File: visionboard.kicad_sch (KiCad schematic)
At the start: 1 part, among them U1 Hirose DF40C-100DS-0.4V

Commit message: microSD card
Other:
- added sheet MicroSD Card (MicroSD.kicad_sch)
- added sheet RJ45 (RJ45.kicad_sch)
- moved on the sheet: U1A, U1B, U1C

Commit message: usb work cont
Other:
- sheet MicroSD Card renamed USB2
- sheet USB2: file MicroSD.kicad_sch -> USB2.kicad_sch
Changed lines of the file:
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@@
 			(color 0 0 0 0.0000)
 		)
-		(property "Sheetname" "MicroSD Card"
+		(property "Sheetname" "USB2"
 			(at 0 304.0884 0)
 			(effects
@@
 			)
 		)
-		(property "Sheetfile" "MicroSD.kicad_sch"
+		(property "Sheetfile" "USB2.kicad_sch"
 			(at 0 337.1346 0)
 			(effects

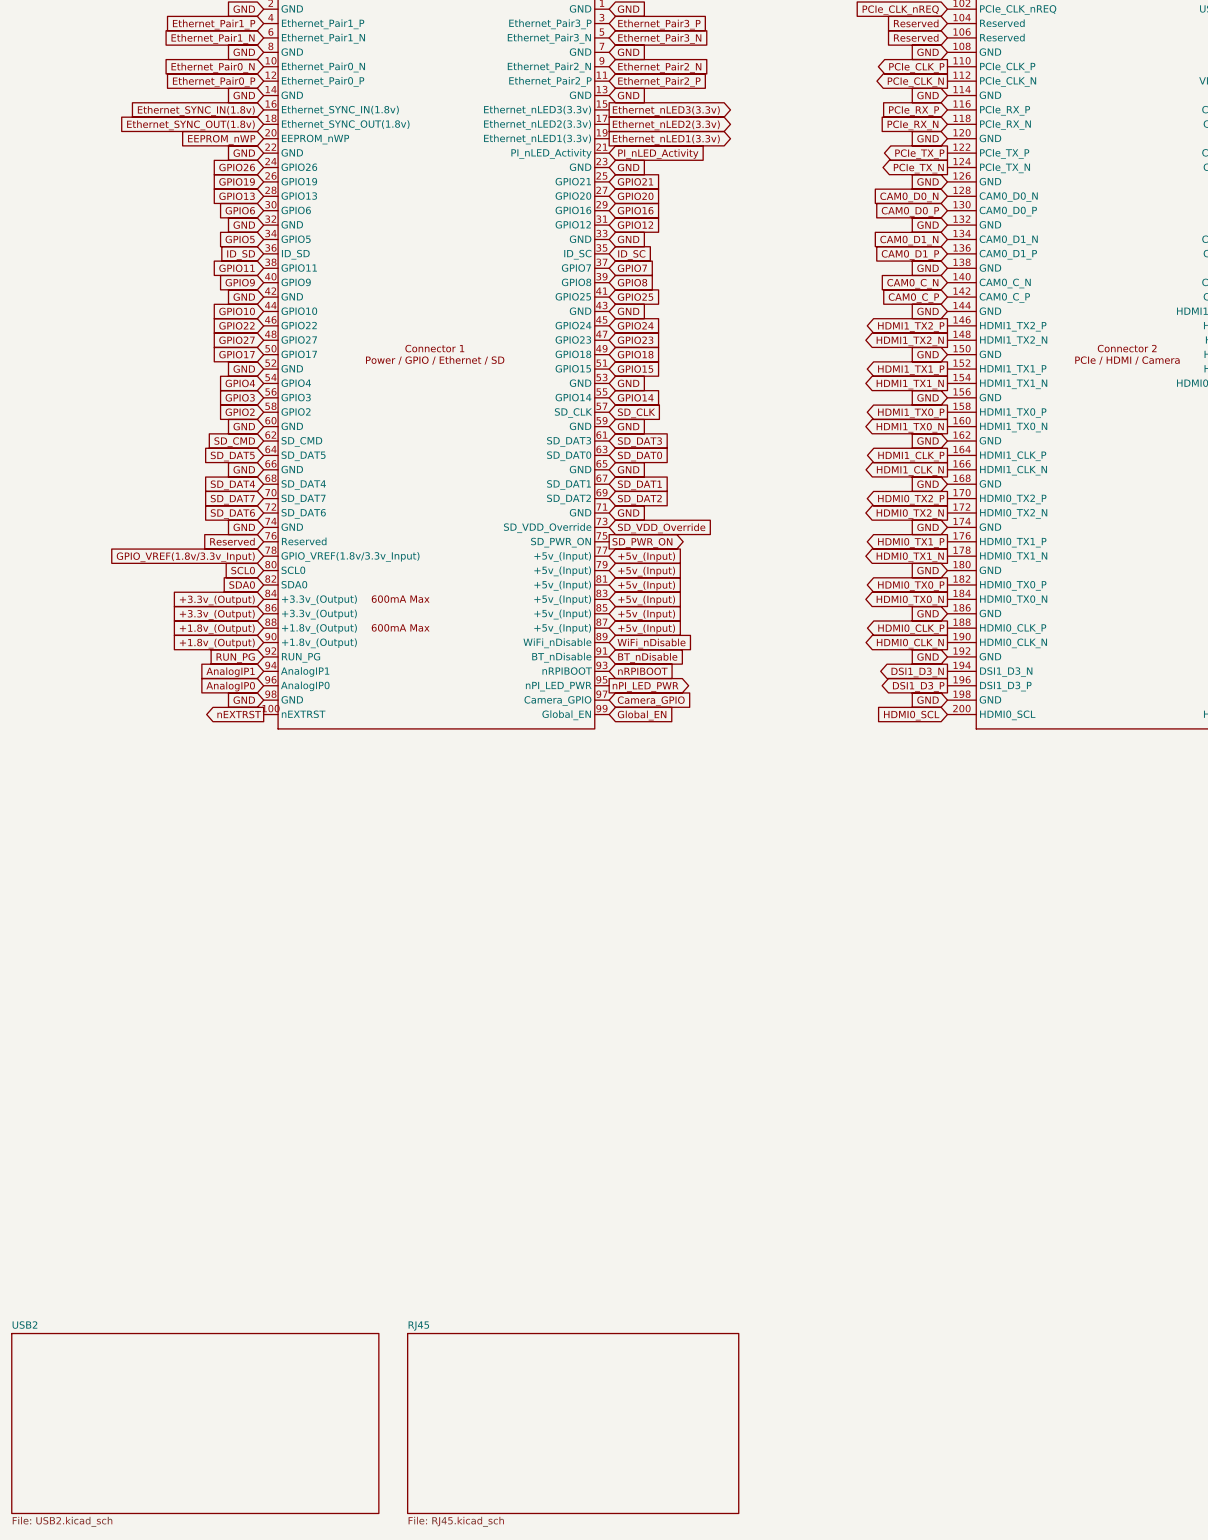
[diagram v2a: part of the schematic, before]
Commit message: usb2 fixes and usb3 started
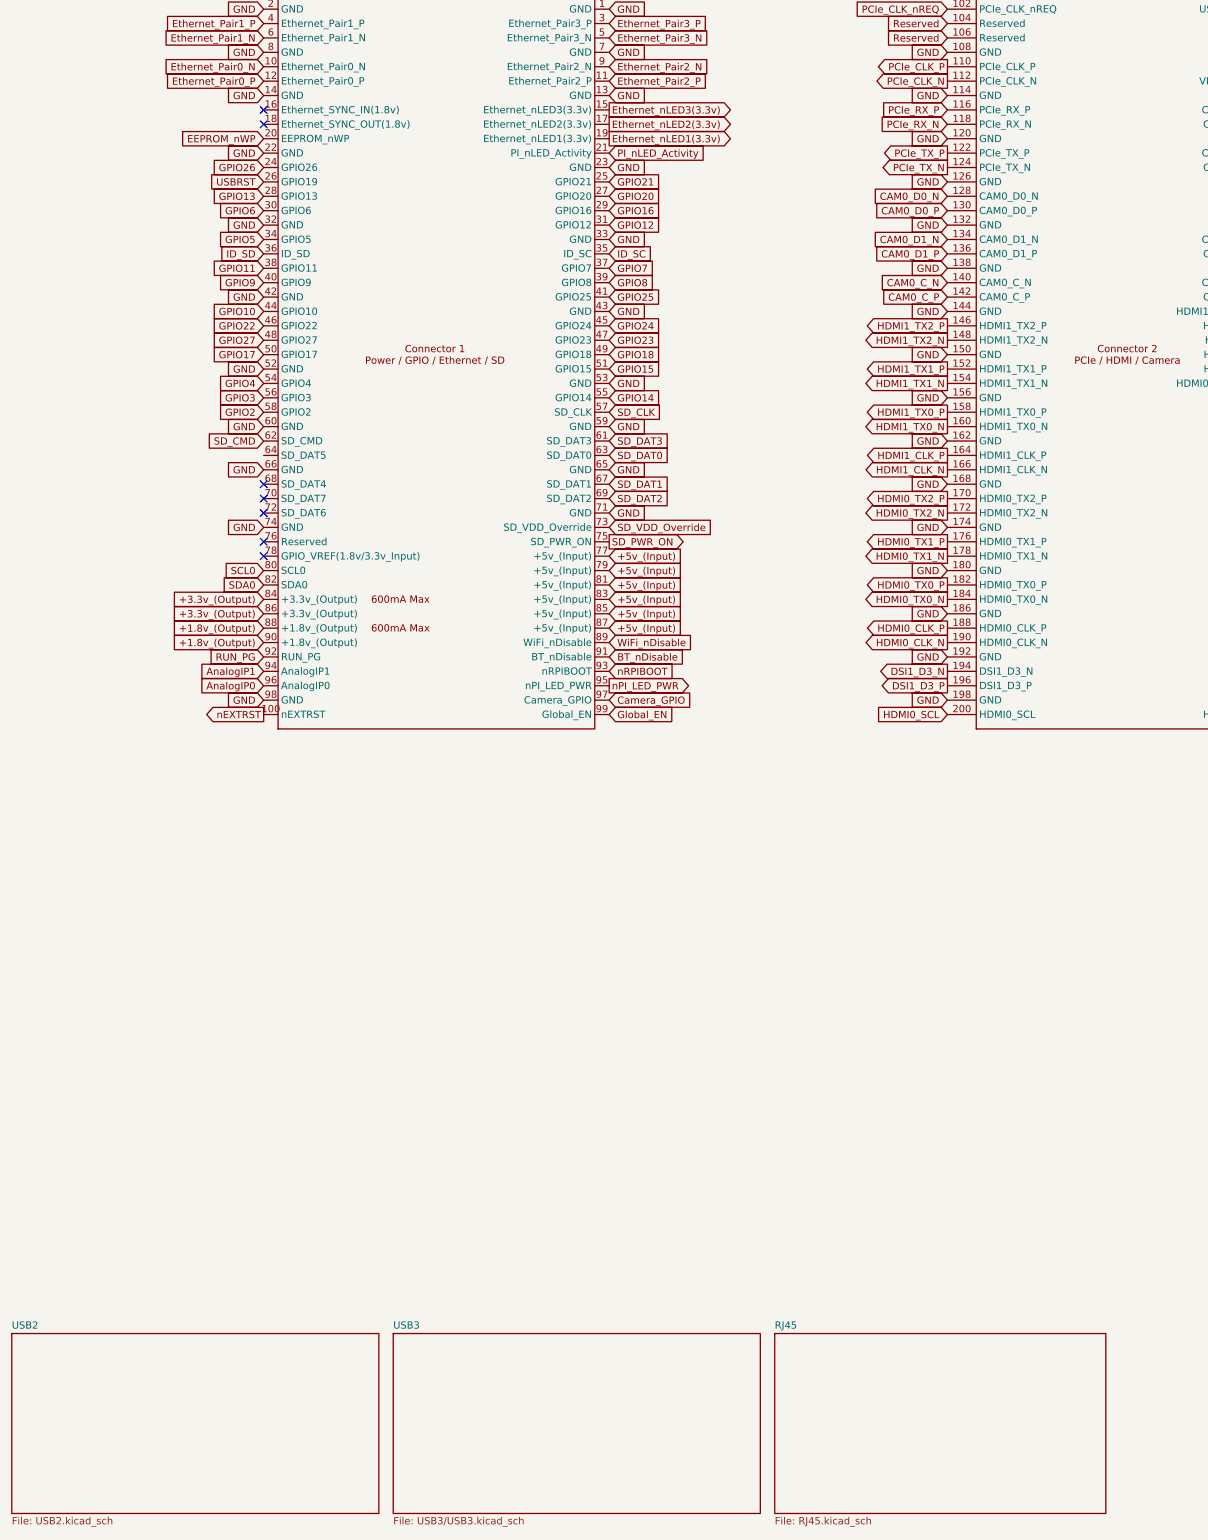
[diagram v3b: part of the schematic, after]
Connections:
- net Reserved: no longer U1.76 (Reserved)
- net Ethernet_SYNC_IN(1.8v): no longer names the net of U1.16 (Ethernet_SYNC_IN(1.8v))
- net Ethernet_SYNC_OUT(1.8v): no longer names the net of U1.18 (Ethernet_SYNC_OUT(1.8v))
- net GPIO19 renamed USBRST
- net GPIO_VREF(1.8v/3.3v_Input): no longer names the net of U1.78 (GPIO_VREF(1.8v/3.3v_Input))
- net SD_DAT4: no longer names the net of U1.68 (SD_DAT4)
- net SD_DAT5: no longer names the net of U1.64 (SD_DAT5)
- net SD_DAT6: no longer names the net of U1.72 (SD_DAT6)
- net SD_DAT7: no longer names the net of U1.70 (SD_DAT7)
- no-connect marks 0 -> 7
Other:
- added sheet USB3 (USB3/USB3.kicad_sch)
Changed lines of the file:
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@@
 	(generator_version "9.0")
 	(paper "A3")
+	(no_connect
+		(at 44.45 160.02)
+	)
+	(no_connect
+		(at 44.45 91.44)
+	)
+	(no_connect
+		(at 44.45 157.48)
+	)
+	(no_connect
+		(at 44.45 88.9)
+	)
+	(no_connect
+		(at 44.45 154.94)
+	)
+	(no_connect
+		(at 44.45 165.1)
+	)
+	(no_connect
+		(at 44.45 167.64)
+	)
 	(global_label "GND"
 		(shape input)
@@
 		)
 	)
-	(global_label "SD_DAT4"
-		(shape input)
-		(at 44.45 154.94 180)
-		(effects
-			(font
-				(size 1.27 1.27)
-			)
-			(justify right)
-		)
-		(property "Intersheetrefs" "${INTERSHEET_REFS}"
-			(at 44.45 154.94 0)
-			(effects
-				(font
-					(size 1.27 1.27)
-				)
-				(hide yes)
-			)
-		)
-	)
 	(global_label "USB3_HOST1_SSRXN"
 		(shape input)
@@
 		)
 	)
-	(global_label "SD_DAT5"
-		(shape input)
-		(at 44.45 149.86 180)
-		(effects
-			(font
-				(size 1.27 1.27)
-			)
-			(justify right)
-		)
-		(property "Intersheetrefs" "${INTERSHEET_REFS}"
-			(at 44.45 149.86 0)
-			(effects
-				(font
-					(size 1.27 1.27)
-				)
-				(hide yes)
-			)
-		)
-	)
 	(global_label "RSVD"
 		(shape input)
@@
 		)
 	)
-	(global_label "Reserved"
-		(shape input)
-		(at 44.45 165.1 180)
-		(effects
-			(font
-				(size 1.27 1.27)
-			)
-			(justify right)
-		)
-		(property "Intersheetrefs" "${INTERSHEET_REFS}"
-			(at 44.45 165.1 0)
-			(effects
-				(font
-					(size 1.27 1.27)
-				)
-				(hide yes)
-			)
-		)
-	)
 	(global_label "CAM1_C_N"
 		(shape input)
@@
 		)
 	)
-	(global_label "Ethernet_SYNC_OUT(1.8v)"
-		(shape input)
-		(at 44.45 91.44 180)
-		(effects
-			(font
-				(size 1.27 1.27)
-			)
-			(justify right)
-		)
-		(property "Intersheetrefs" "${INTERSHEET_REFS}"
-			(at 44.45 91.44 0)
-			(effects
-				(font
-					(size 1.27 1.27)
-				)
-				(hide yes)
-			)
-		)
-	)
 	(global_label "GPIO17"
 		(shape input)
@@
 		)
 	)
-	(global_label "SD_DAT7"
-		(shape input)
-		(at 44.45 157.48 180)
-		(effects
-			(font
-				(size 1.27 1.27)
-			)
-			(justify right)
-		)
-		(property "Intersheetrefs" "${INTERSHEET_REFS}"
-			(at 44.45 157.48 0)
-			(effects
-				(font
-					(size 1.27 1.27)
-				)
-				(hide yes)
-			)
-		)
-	)
 	(global_label "GPIO8"
 		(shape input)
@@
 		)
 	)
-	(global_label "SD_DAT6"
-		(shape input)
-		(at 44.45 160.02 180)
-		(effects
-			(font
-				(size 1.27 1.27)
-			)
-			(justify right)
-		)
-		(property "Intersheetrefs" "${INTERSHEET_REFS}"
-			(at 44.45 160.02 0)
-			(effects
-				(font
-					(size 1.27 1.27)
-				)
-				(hide yes)
-			)
-		)
-	)
 	(global_label "DSI0_D0_P"
 		(shape output)
@@
 		)
 	)
-	(global_label "Ethernet_SYNC_IN(1.8v)"
-		(shape input)
-		(at 44.45 88.9 180)
-		(effects
-			(font
-				(size 1.27 1.27)
-			)
-			(justify right)
-		)
-		(property "Intersheetrefs" "${INTERSHEET_REFS}"
-			(at 44.45 88.9 0)
-			(effects
-				(font
-					(size 1.27 1.27)
-				)
-				(hide yes)
-			)
-		)
-	)
 	(global_label "HDMI0_HOTPLUG"
 		(shape input)
@@
 		)
 	)
-	(global_label "GPIO_VREF(1.8v/3.3v_Input)"
-		(shape input)
-		(at 44.45 167.64 180)
-		(effects
-			(font
-				(size 1.27 1.27)
-			)
-			(justify right)
-		)
-		(property "Intersheetrefs" "${INTERSHEET_REFS}"
-			(at 44.45 167.64 0)
-			(effects
-				(font
-					(size 1.27 1.27)
-				)
-				(hide yes)
-			)
-		)
-	)
 	(global_label "HDMI1_CLK_N"
 		(shape output)
@@
 		)
 	)
-	(global_label "GPIO19"
+	(global_label "USBRST"
 		(shape input)
 		(at 44.45 101.6 180)
@@
 	)
 	(sheet
-		(at 69.85 304.8)
+		(at 134.62 304.8)
 		(size 58.42 31.75)
 		(exclude_from_sim no)
@@
 		)
 		(property "Sheetname" "RJ45"
-			(at 69.85 304.0884 0)
+			(at 134.62 304.0884 0)
 			(effects
 				(font
@@
 		)
 		(property "Sheetfile" "RJ45.kicad_sch"
-			(at 69.85 337.1346 0)
+			(at 134.62 337.1346 0)
 			(effects
 				(font
@@
 				)
 			)
+		)
+	)
+	(sheet
+		(at 67.31 304.8)
+		(size 64.77 31.75)
+		(exclude_from_sim no)
+		(in_bom yes)
+		(on_board yes)
+		(dnp no)
+		(fields_autoplaced yes)
+		(stroke
+			(width 0.1524)
+			(type solid)
+		)
+		(fill
+			(color 0 0 0 0.0000)
+		)
+		(property "Sheetname" "USB3"
+			(at 67.31 304.0884 0)
+			(effects
+				(font
+					(size 1.27 1.27)
+				)
+				(justify left bottom)
+			)
+		)
+		(property "Sheetfile" "USB3/USB3.kicad_sch"
+			(at 67.31 337.1346 0)
+			(effects
+				(font
+					(size 1.27 1.27)
+				)
+				(justify left top)
+			)
+		)
+		(instances
+			(project "visionboard"
+				(path "/600da949-f681-489f-915b-075a1ebe377b"
+					(page "4")
+				)
+			)

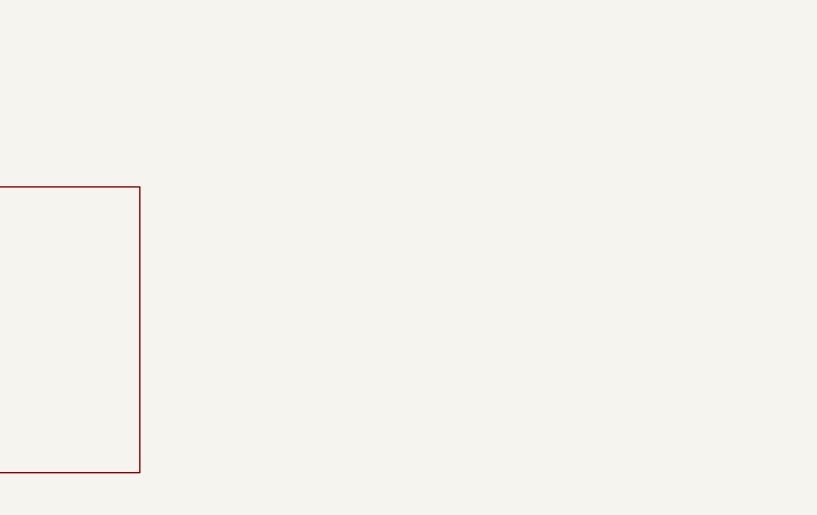
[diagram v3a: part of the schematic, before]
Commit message: added power page
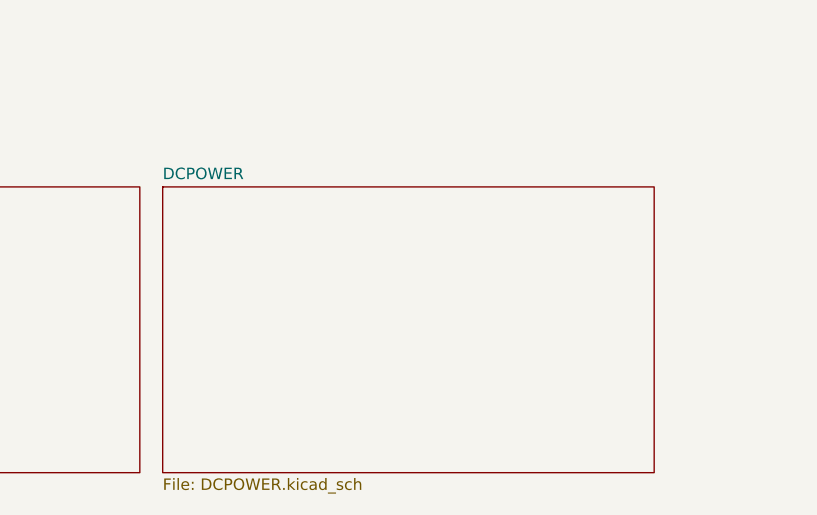
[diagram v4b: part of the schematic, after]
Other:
- added sheet DCPOWER (DCPOWER.kicad_sch)
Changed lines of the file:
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@@
+	)
+	(sheet
+		(at 195.58 304.8)
+		(size 54.61 31.75)
+		(exclude_from_sim no)
+		(in_bom yes)
+		(on_board yes)
+		(dnp no)
+		(fields_autoplaced yes)
+		(stroke
+			(width 0.1524)
+			(type solid)
+		)
+		(fill
+			(color 0 0 0 0.0000)
+		)
+		(property "Sheetname" "DCPOWER"
+			(at 195.58 304.0884 0)
+			(effects
+				(font
+					(size 1.27 1.27)
+				)
+				(justify left bottom)
+			)
+		)
+		(property "Sheetfile" "DCPOWER.kicad_sch"
+			(at 195.58 337.1346 0)
+			(effects
+				(font
+					(size 1.27 1.27)
+				)
+				(justify left top)
+			)
+		)
+		(instances
+			(project "visionboard"
+				(path "/600da949-f681-489f-915b-075a1ebe377b"
+					(page "11")
+				)
+			)
+		)
 	)
 	(sheet
